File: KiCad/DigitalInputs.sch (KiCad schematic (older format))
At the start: 58 parts, among them J1 DI1, J2 DI2, J3 DI3, J4 DI4, J5 DI5, J6 DI6, J7 DI7, J8 DI8, U1 LTV-354T, U2 LTV-354T, U3 LTV-354T, U4 LTV-354T, U5 LTV-354T, U6 LTV-354T, U7 LTV-354T, U8 LTV-354T

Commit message: Analog inputs
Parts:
- removed J?: Screw_Terminal_1x08, symbol Screw_Terminal_1x08
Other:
- note added: "Select based on input voltage.\nMax 50mA.\n1k should allow for \nvoltages 3.3 - 48V"
- note removed: "Select based on input voltage.\nMax 50mA.\n1k should allow for voltages up to 3.3 - 48V"
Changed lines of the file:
@@
 LIBS:spark_esp32thing
 LIBS:HAP-IO-Card-cache
-EELAYER 25 0
+EELAYER 26 0
 EELAYER END
 $Descr A4 11693 8268
@@
 $EndDescr
 $Comp
-L +3V3 #PWR10
+L +3V3 #PWR01
 U 1 1 59181D39
 P 7250 2450
-F 0 "#PWR10" H 7250 2300 50  0001 C CNN
+F 0 "#PWR01" H 7250 2300 50  0001 C CNN
 F 1 "+3V3" H 7250 2590 50  0000 C CNN
 F 2 "" H 7250 2450 50  0001 C CNN
@@
 $EndComp
 $Comp
-L +3V3 #PWR9
+L +3V3 #PWR02
 U 1 1 59181DA4
 P 5950 3300
-F 0 "#PWR9" H 5950 3150 50  0001 C CNN
+F 0 "#PWR02" H 5950 3150 50  0001 C CNN
 F 1 "+3V3" H 5950 3440 50  0000 C CNN
 F 2 "" H 5950 3300 50  0001 C CNN
@@
 $EndComp
 $Comp
-L GND #PWR3
+L GND #PWR03
 U 1 1 59181E0C
 P 4400 3650
-F 0 "#PWR3" H 4400 3400 50  0001 C CNN
+F 0 "#PWR03" H 4400 3400 50  0001 C CNN
 F 1 "GND" H 4400 3500 50  0000 C CNN
 F 2 "" H 4400 3650 50  0001 C CNN
@@
 $EndComp
 $Comp
-L GND #PWR6
+L GND #PWR04
 U 1 1 59181E12
 P 4400 5150
-F 0 "#PWR6" H 4400 4900 50  0001 C CNN
+F 0 "#PWR04" H 4400 4900 50  0001 C CNN
 F 1 "GND" H 4400 5000 50  0000 C CNN
 F 2 "" H 4400 5150 50  0001 C CNN
@@
 $EndComp
 $Comp
-L GND #PWR8
+L GND #PWR05
 U 1 1 59181E18
 P 4400 6150
-F 0 "#PWR8" H 4400 5900 50  0001 C CNN
+F 0 "#PWR05" H 4400 5900 50  0001 C CNN
 F 1 "GND" H 4400 6000 50  0000 C CNN
 F 2 "" H 4400 6150 50  0001 C CNN
@@
 $EndComp
 $Comp
-L GND #PWR7
+L GND #PWR06
 U 1 1 59181E1E
 P 4400 5650
-F 0 "#PWR7" H 4400 5400 50  0001 C CNN
+F 0 "#PWR06" H 4400 5400 50  0001 C CNN
 F 1 "GND" H 4400 5500 50  0000 C CNN
 F 2 "" H 4400 5650 50  0001 C CNN
@@
 $EndComp
 $Comp
-L GND #PWR5
+L GND #PWR07
 U 1 1 59181E24
 P 4400 4650
-F 0 "#PWR5" H 4400 4400 50  0001 C CNN
+F 0 "#PWR07" H 4400 4400 50  0001 C CNN
 F 1 "GND" H 4400 4500 50  0000 C CNN
 F 2 "" H 4400 4650 50  0001 C CNN
@@
 $EndComp
 $Comp
-L GND #PWR4
+L GND #PWR08
 U 1 1 59181E2A
 P 4400 4150
-F 0 "#PWR4" H 4400 3900 50  0001 C CNN
+F 0 "#PWR08" H 4400 3900 50  0001 C CNN
 F 1 "GND" H 4400 4000 50  0000 C CNN
 F 2 "" H 4400 4150 50  0001 C CNN
@@
 $EndComp
 $Comp
-L GND #PWR2
+L GND #PWR09
 U 1 1 59181E30
 P 4400 3150
-F 0 "#PWR2" H 4400 2900 50  0001 C CNN
+F 0 "#PWR09" H 4400 2900 50  0001 C CNN
 F 1 "GND" H 4400 3000 50  0000 C CNN
 F 2 "" H 4400 3150 50  0001 C CNN
@@
 $EndComp
 $Comp
-L GND #PWR1
+L GND #PWR010
 U 1 1 59181EE6
 P 4400 2600
-F 0 "#PWR1" H 4400 2350 50  0001 C CNN
+F 0 "#PWR010" H 4400 2350 50  0001 C CNN
 F 1 "GND" H 4400 2450 50  0000 C CNN
 F 2 "" H 4400 2600 50  0001 C CNN
@@
 DI8
 $Comp
-L +3V3 #PWR11
+L +3V3 #PWR011
 U 1 1 59194C57
 P 7250 2750
-F 0 "#PWR11" H 7250 2600 50  0001 C CNN
+F 0 "#PWR011" H 7250 2600 50  0001 C CNN
 F 1 "+3V3" H 7250 2890 50  0000 C CNN
 F 2 "" H 7250 2750 50  0001 C CNN
@@
 	6900 2750 6950 2750
 $Comp
-L +3V3 #PWR12
+L +3V3 #PWR012
 U 1 1 5919594E
 P 7250 3050
-F 0 "#PWR12" H 7250 2900 50  0001 C CNN
+F 0 "#PWR012" H 7250 2900 50  0001 C CNN
 F 1 "+3V3" H 7250 3190 50  0000 C CNN
 F 2 "" H 7250 3050 50  0001 C CNN
@@
 	6900 3050 6950 3050
 $Comp
-L +3V3 #PWR13
+L +3V3 #PWR013
 U 1 1 59195A2F
 P 7250 3350
-F 0 "#PWR13" H 7250 3200 50  0001 C CNN
+F 0 "#PWR013" H 7250 3200 50  0001 C CNN
 F 1 "+3V3" H 7250 3490 50  0000 C CNN
 F 2 "" H 7250 3350 50  0001 C CNN
@@
 	6900 3350 6950 3350
 $Comp
-L +3V3 #PWR14
+L +3V3 #PWR014
 U 1 1 59195AD5
 P 7250 3650
-F 0 "#PWR14" H 7250 3500 50  0001 C CNN
+F 0 "#PWR014" H 7250 3500 50  0001 C CNN
 F 1 "+3V3" H 7250 3790 50  0000 C CNN
 F 2 "" H 7250 3650 50  0001 C CNN
@@
 	6900 3650 6950 3650
 $Comp
-L +3V3 #PWR15
+L +3V3 #PWR015
 U 1 1 59195B7D
 P 7250 3950
-F 0 "#PWR15" H 7250 3800 50  0001 C CNN
+F 0 "#PWR015" H 7250 3800 50  0001 C CNN
 F 1 "+3V3" H 7250 4090 50  0000 C CNN
 F 2 "" H 7250 3950 50  0001 C CNN
@@
 	6900 3950 6950 3950
 $Comp
-L +3V3 #PWR16
+L +3V3 #PWR016
 U 1 1 59195C13
 P 7250 4250
-F 0 "#PWR16" H 7250 4100 50  0001 C CNN
+F 0 "#PWR016" H 7250 4100 50  0001 C CNN
 F 1 "+3V3" H 7250 4390 50  0000 C CNN
 F 2 "" H 7250 4250 50  0001 C CNN
@@
 	6900 4250 6950 4250
 $Comp
-L +3V3 #PWR17
+L +3V3 #PWR017
 U 1 1 591960FF
 P 7250 4550
-F 0 "#PWR17" H 7250 4400 50  0001 C CNN
+F 0 "#PWR017" H 7250 4400 50  0001 C CNN
 F 1 "+3V3" H 7250 4690 50  0000 C CNN
 F 2 "" H 7250 4550 50  0001 C CNN
@@
 Wire Wire Line
 	3350 6150 3650 6150
-Text Notes 3550 2300 1    50   ~ 0
-Select based on input voltage.\nMax 50mA.\n1k should allow for voltages up to 3.3 - 48V
-$Comp
-L Screw_Terminal_1x08 J?
-U 1 1 591A979B
-P 2300 3150
-F 0 "J?" H 2300 4000 50  0000 C TNN
-F 1 "Screw_Terminal_1x08" V 2150 3150 50  0000 C TNN
-F 2 "" H 2300 2325 50  0001 C CNN
-F 3 "" H 2275 3750 50  0001 C CNN
-	1    2300 3150
-	1    0    0    -1
-$EndComp
+Text Notes 3600 2250 1    50   ~ 0
+Select based on input voltage.\nMax 50mA.\n1k should allow for \nvoltages 3.3 - 48V
 $EndSCHEMATC

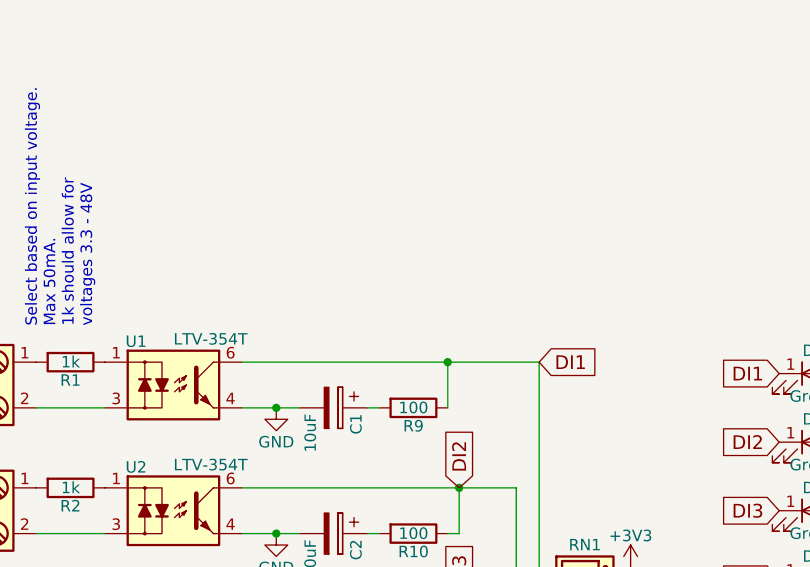
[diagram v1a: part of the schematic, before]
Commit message: Added power supply
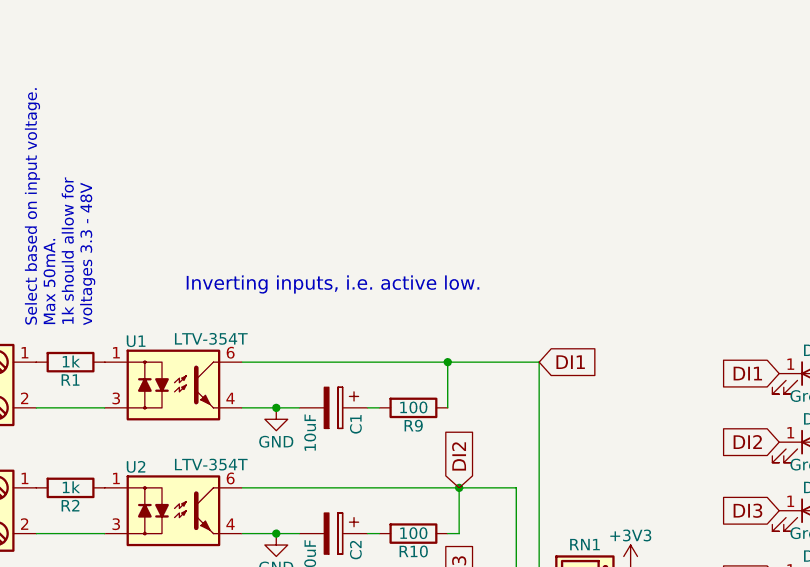
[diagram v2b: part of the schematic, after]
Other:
- note added: "Inverting inputs, i.e. active low."
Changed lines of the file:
@@
 LIBS:valves
 LIBS:spark_esp32thing
+LIBS:Power_Management
+LIBS:dc-dc
+LIBS:diode
+LIBS:ESD_Protection
+LIBS:SRR1260-330M
 LIBS:HAP-IO-Card-cache
 EELAYER 26 0
@@
 $Descr A4 11693 8268
 encoding utf-8
-Sheet 2 4
+Sheet 2 6
 Title ""
 Date ""
@@
 Text Notes 3600 2250 1    50   ~ 0
 Select based on input voltage.\nMax 50mA.\n1k should allow for \nvoltages 3.3 - 48V
+Text Notes 4000 2100 0    60   ~ 0
+Inverting inputs, i.e. active low.
 $EndSCHEMATC

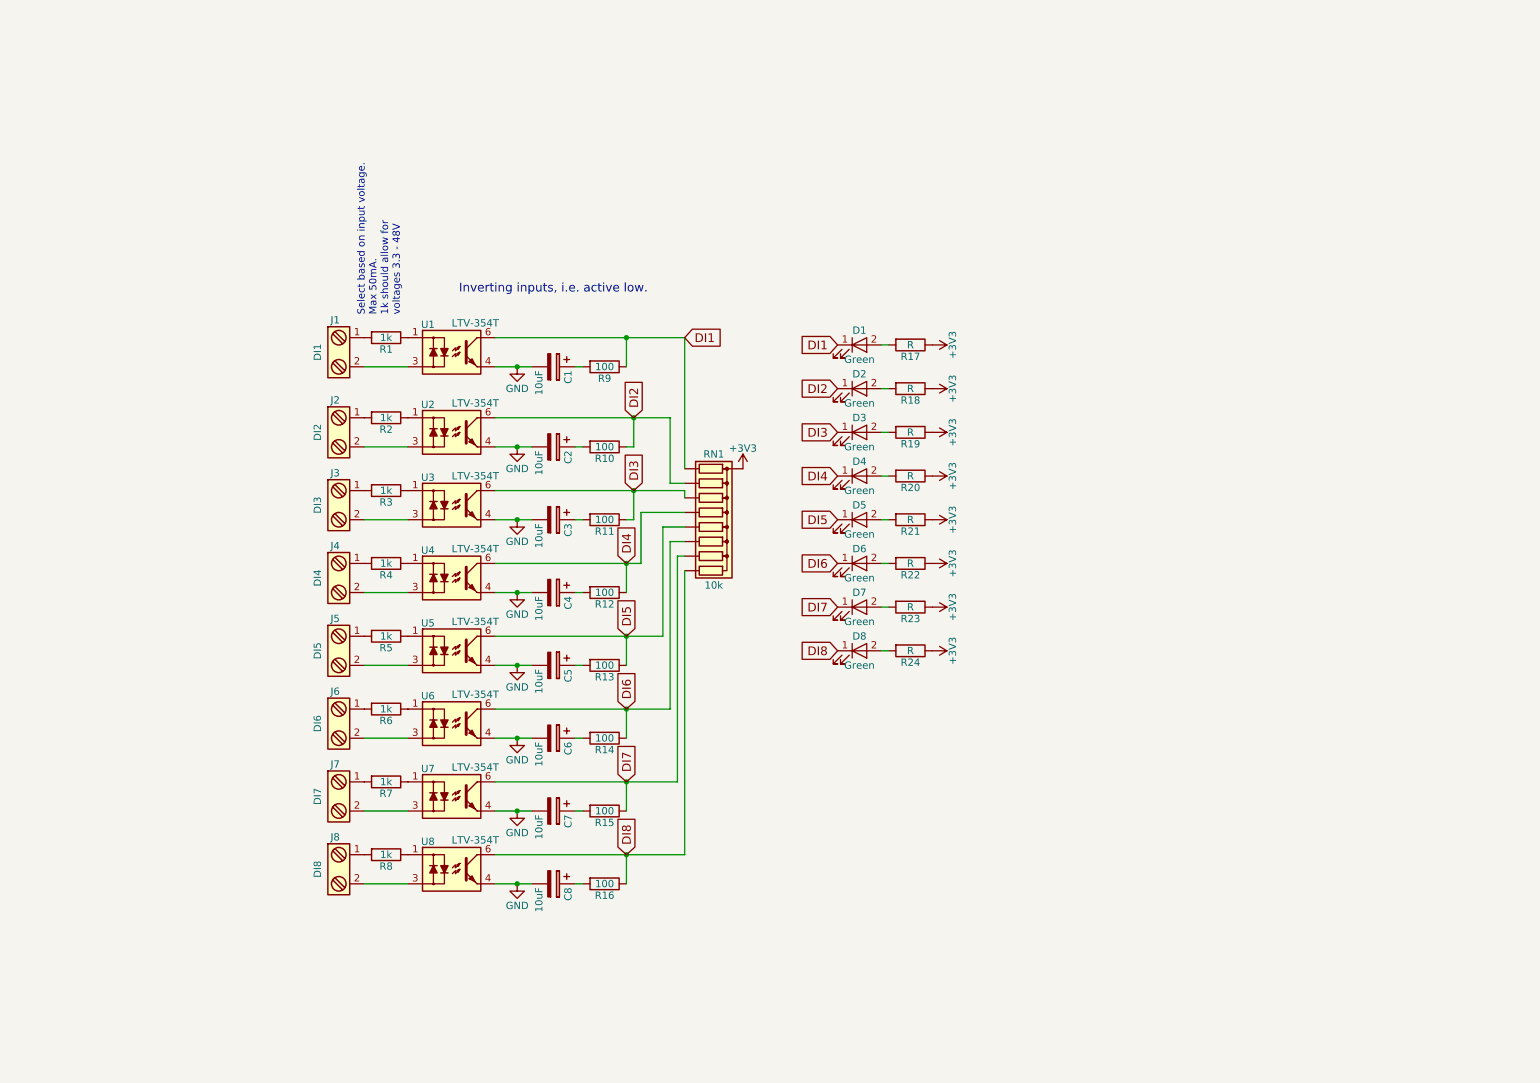
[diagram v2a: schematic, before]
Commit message: Use I2C for I/O
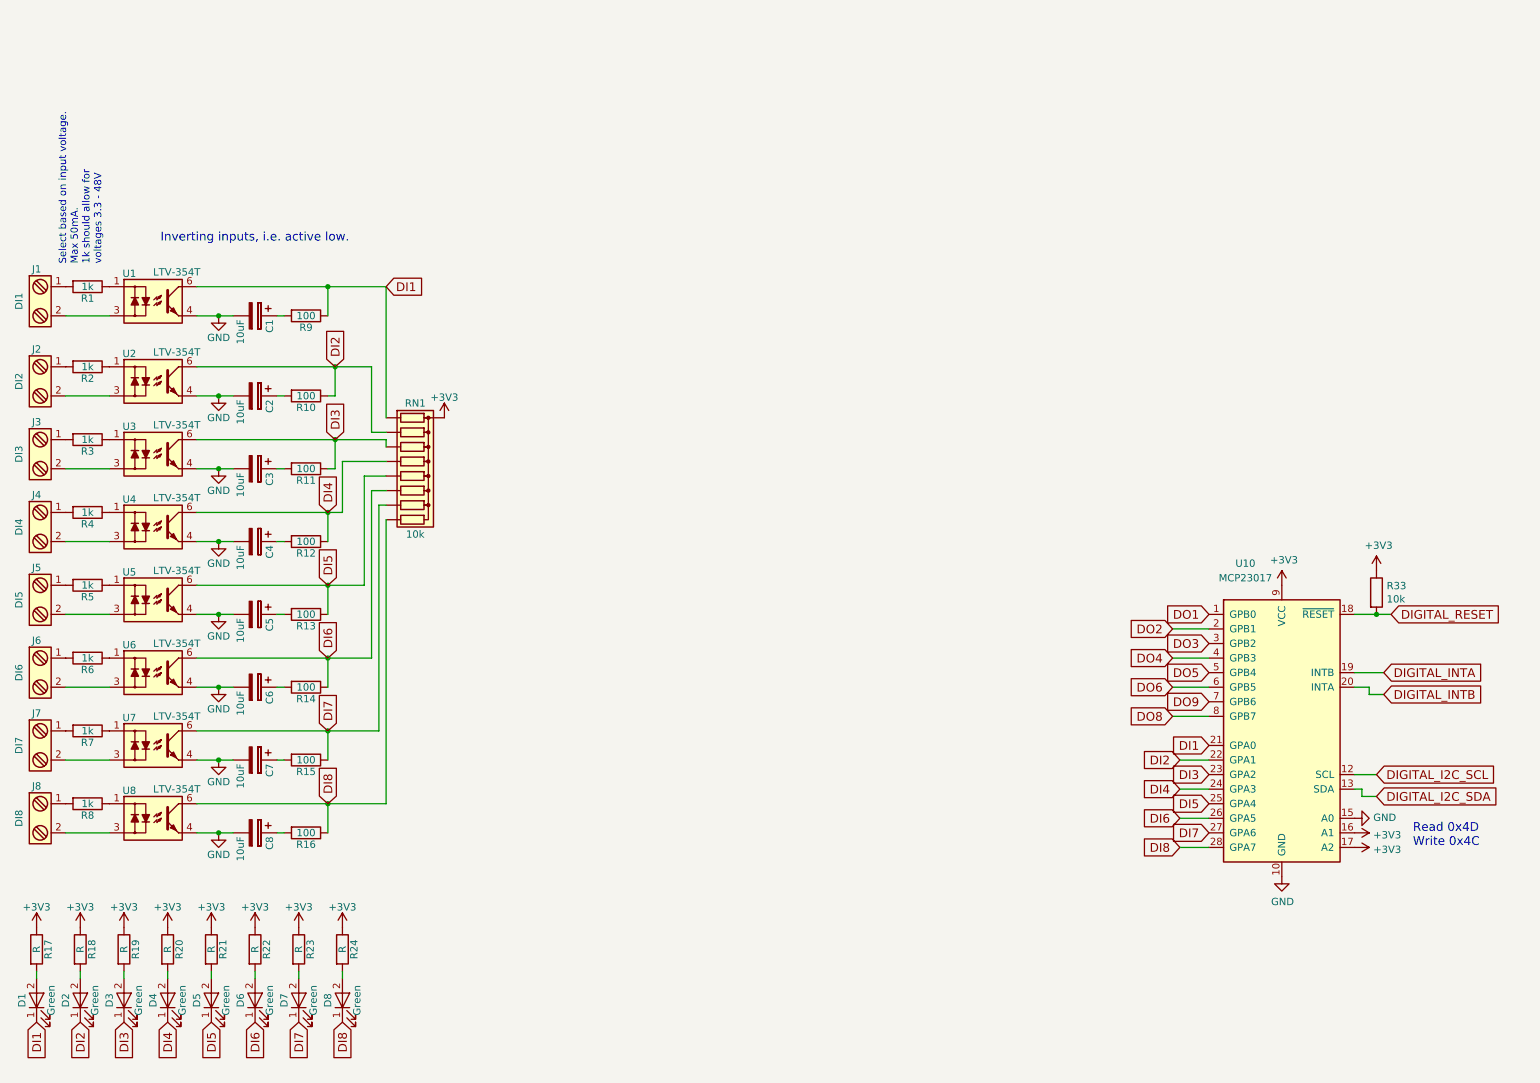
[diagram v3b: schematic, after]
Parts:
- added R33: 10k, Resistors_SMD:R_0805, symbol R
- added U10: MCP23017, Housings_SOIC:SOIC-28W_7.5x17.9mm_Pitch1.27mm, symbol MCP23017
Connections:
- net +3V3: now also R33.1, U10.16 (A1), U10.17 (A2), U10.9 (VCC)
- net DI1: now also U10.21 (GPA0)
- net DI2: now also U10.22 (GPA1)
- net DI3: now also U10.23 (GPA2)
- net DI4: now also U10.24 (GPA3)
- net DI5: now also U10.25 (GPA4)
- net DI6: now also U10.26 (GPA5)
- net DI7: now also U10.27 (GPA6)
- net DI8: now also U10.28 (GPA7)
- net GND: now also U10.10 (GND), U10.15 (A0)
- new net DIGITAL_I2C_SCL: U10.12 (SCL)
- new net DIGITAL_I2C_SDA: U10.13 (SDA)
- new net DIGITAL_INTA: U10.19 (INTB)
- new net DIGITAL_INTB: U10.20 (INTA)
- new net DIGITAL_RESET: R33.2, U10.18 (~RESET)
- new net DO1: U10.1 (GPB0)
- new net DO2: U10.2 (GPB1)
- new net DO3: U10.3 (GPB2)
- new net DO4: U10.4 (GPB3)
- new net DO5: U10.5 (GPB4)
- new net DO6: U10.6 (GPB5)
- new net DO8: U10.8 (GPB7)
- new net DO9: U10.7 (GPB6)
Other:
- note added: "Read 0x4D\nWrite 0x4C"
- moved on the sheet: C1, C2, C3, C4, C5, C6, C7, C8, D1, D2, D3, D4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
